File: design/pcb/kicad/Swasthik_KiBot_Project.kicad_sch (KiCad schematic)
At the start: 0 parts

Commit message: Add LCD and STLink schematic sheets, update KiCad project files
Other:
- title: (none) -> Project Architecture
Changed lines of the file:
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@@
 	(paper "A3")
 	(title_block
+		(title "Project Architecture")
 		(date "2025-01-12")
 		(rev "${REVISION}")

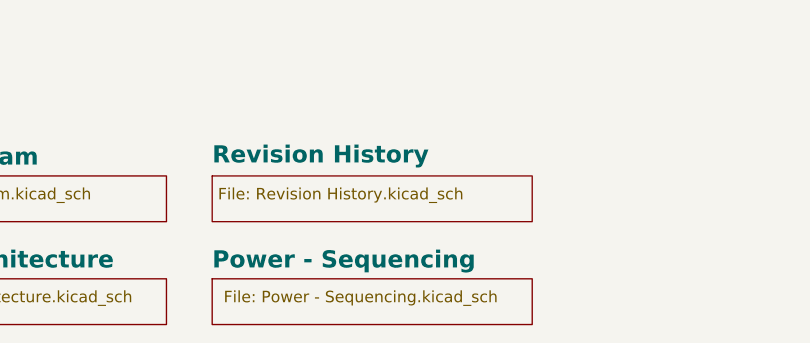
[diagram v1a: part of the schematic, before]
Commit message: Change of USB and STlink label
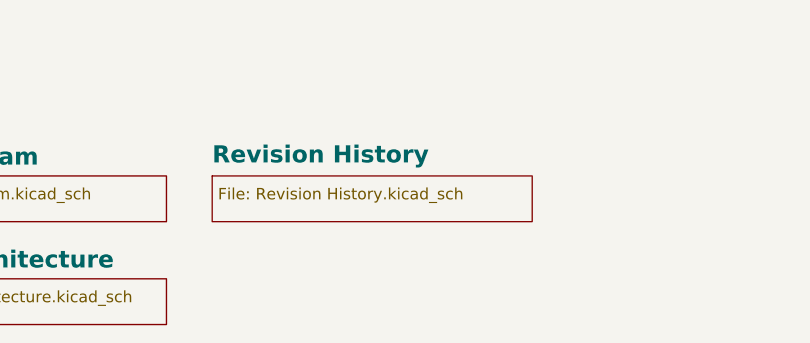
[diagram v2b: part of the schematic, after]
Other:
- removed sheet Power - Sequencing
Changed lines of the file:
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@@
-	)
-	(sheet
-		(at 340.36 313.69)
-		(size 35.56 5.08)
-		(exclude_from_sim no)
-		(in_bom yes)
-		(on_board yes)
-		(dnp no)
-		(stroke
-			(width 0.1524)
-			(type solid)
-		)
-		(fill
-			(color 0 0 0 0.0000)
-		)
-		(property "Sheetname" "Power - Sequencing"
-			(at 340.36 312.6609 0)
-			(effects
-				(font
-					(face "Times New Roman")
-					(size 1.905 1.905)
-					(bold yes)
-					(color 0 0 0 1)
-				)
-				(justify left bottom)
-			)
-		)
-		(property "Sheetfile" "Power - Sequencing.kicad_sch"
-			(at 341.63 314.96 0)
-			(effects
-				(font
-					(face "Arial")
-					(size 1.27 1.27)
-				)
-				(justify left top)
-			)
-		)
-		(instances
-			(project "Swasthik_KiBot_Project"
-				(path "/f9e05184-c88b-4a88-ae9c-ab2bdb32be7c"
-					(page "6")
-				)
-			)
-		)
 	)
 	(sheet
